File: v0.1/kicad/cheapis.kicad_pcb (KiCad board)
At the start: 2 copper layers, 99.9 x 99.9 mm, 25 parts, among them J1 Conn_01x01, SW1 SW_Diode_Combined, SW10 SW_Diode_Combined, SW11 SW_Diode_Combined, SW12 SW_Diode_Combined, SW13 SW_Diode_Combined, SW14 SW_Diode_Combined, SW15 SW_Diode_Combined, SW16 SW_Diode_Combined, SW17 SW_Diode_Combined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

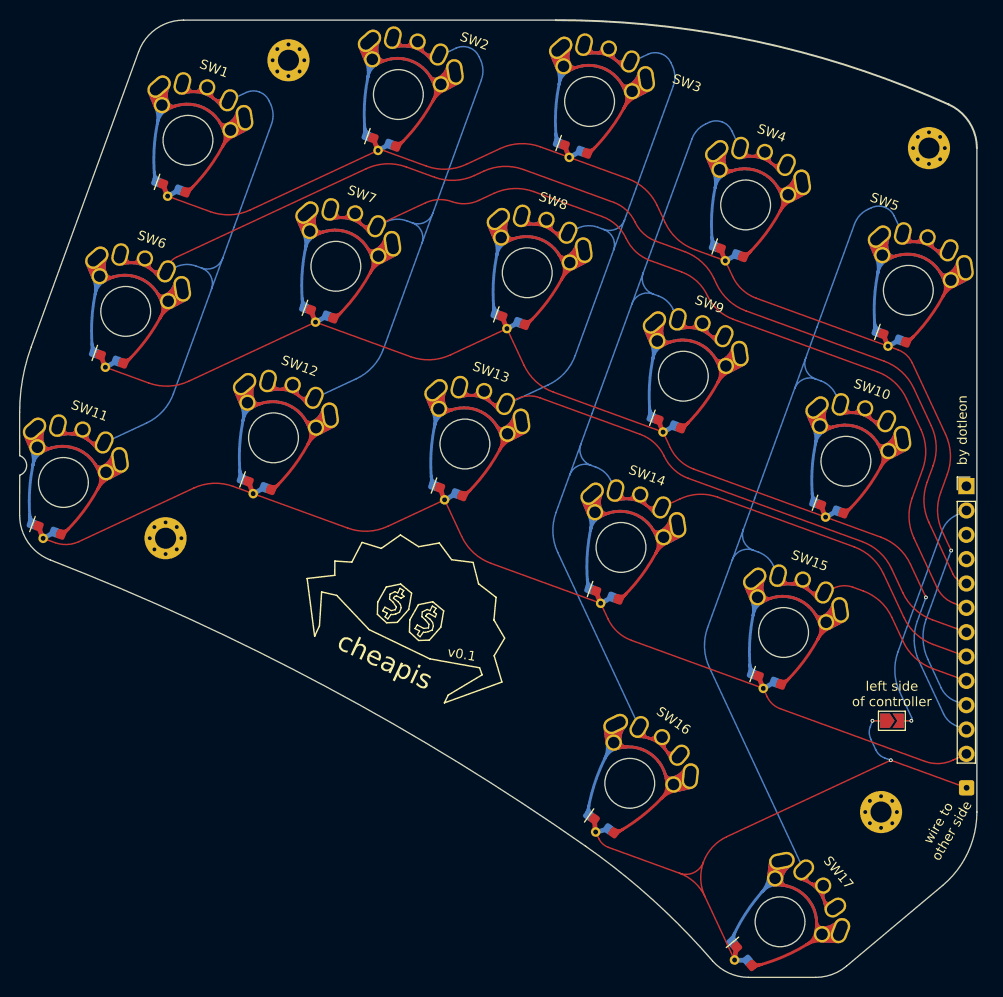
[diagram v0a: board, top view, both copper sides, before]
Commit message: add customized SW_Redragon_LowProfile_1.00u footprint
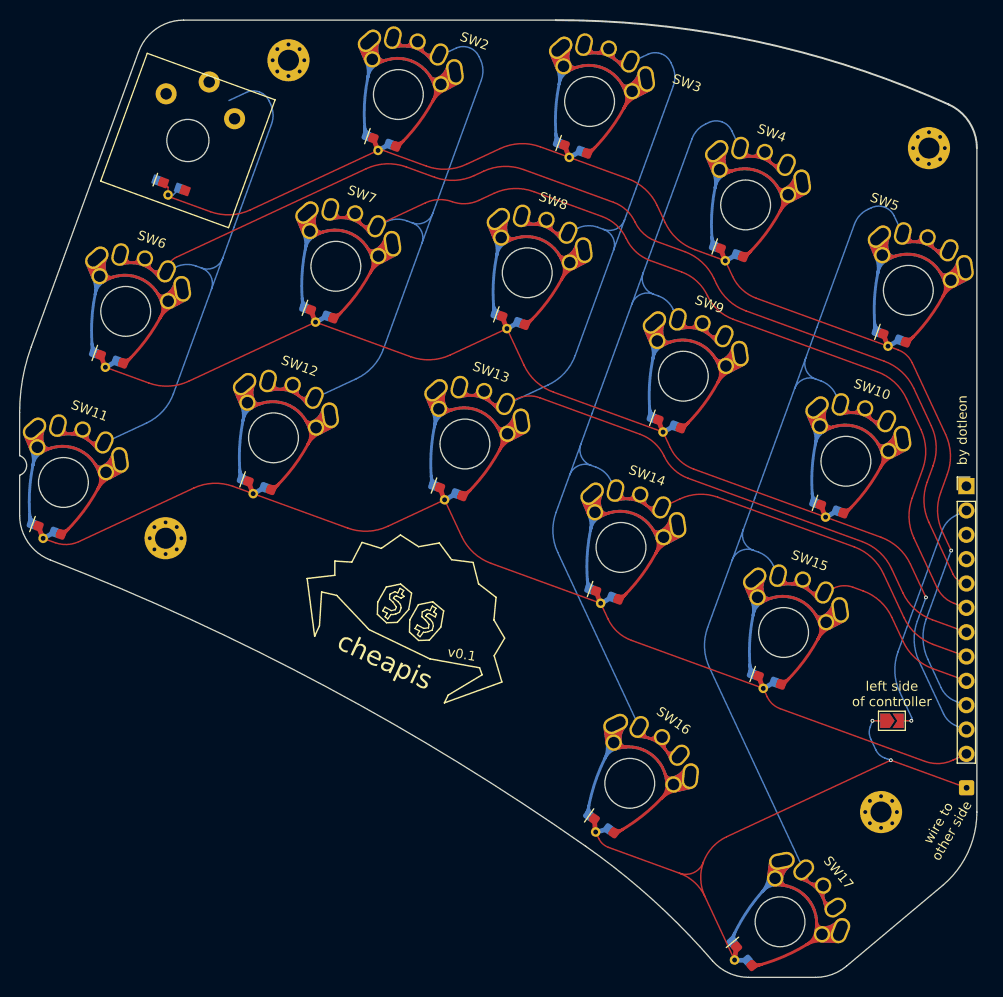
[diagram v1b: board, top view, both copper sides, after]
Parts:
- SW1: footprint dotleon:SW_MX_GATLP_CHOC_reversible -> Redragon:SW_Redragon_LowProfile_PCB_1.00u
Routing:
- net row1: track 127.4 -> 130.4 mm
